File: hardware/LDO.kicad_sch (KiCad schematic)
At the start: 5 parts, among them U1 MCP1826S

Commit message: fixed ERC, made it look pretty
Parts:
- renumbered U1 to U2
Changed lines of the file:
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@@
 		(dnp no)
 		(fields_autoplaced yes)
-		(property "Reference" "U1"
+		(property "Reference" "U2"
 			(at 152.4 56.515 0)
 			(show_name no)
@@
 			(project "PS-HVCarrier"
 				(path "/2365a867-6254-4a7c-9718-f325e0bbac5c/904fa10a-747c-46cf-90d1-33d76069dc5d/d9c02800-502d-4b66-a933-6a0fcb4cc3ad"
-					(reference "U1")
+					(reference "U2")
 					(unit 1)
 				)

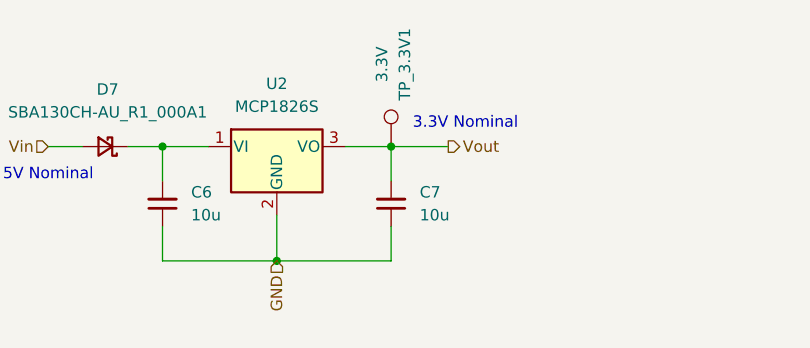
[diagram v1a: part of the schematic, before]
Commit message: updated TP
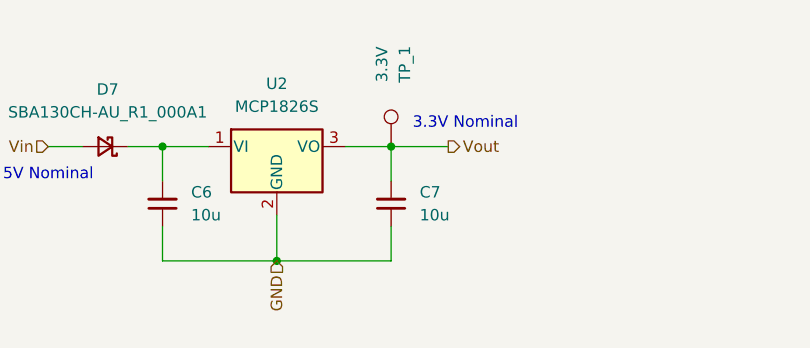
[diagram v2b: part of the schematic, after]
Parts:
- TP_1: renamed from TP_3.3V1; footprint TestPoint:TestPoint_Loop_D1.80mm_Drill1.0mm_Beaded -> TestPoint:TestPoint_THTPad_D3.0mm_Drill1.5mm
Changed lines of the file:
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@@
+			)
+		)
+		(property "LCSC" ""
+			(at 133.35 63.5 0)
+			(hide yes)
+			(show_name no)
+			(do_not_autoplace no)
+			(effects
+				(font
+					(size 1.27 1.27)
+				)
 			)
 		)
@@
 			)
 		)
+		(property "LCSC" ""
+			(at 165.1 69.85 0)
+			(hide yes)
+			(show_name no)
+			(do_not_autoplace no)
+			(effects
+				(font
+					(size 1.27 1.27)
+				)
+			)
+		)
 		(pin "1"
 		)
@@
 		(in_pos_files yes)
 		(dnp no)
-		(property "Reference" "TP_3.3V1"
+		(property "Reference" "TP_1"
 			(at 166.624 54.356 90)
 			(show_name no)
@@
 			)
 		)
-		(property "Footprint" "TestPoint:TestPoint_Loop_D1.80mm_Drill1.0mm_Beaded"
+		(property "Footprint" "TestPoint:TestPoint_THTPad_D3.0mm_Drill1.5mm"
 			(at 170.18 63.5 0)
 			(hide yes)
@@
 		(property "Vf" ""
 			(at 165.1 63.5 0)
+			(show_name no)
+			(do_not_autoplace no)
+			(effects
+				(font
+					(size 1.27 1.27)
+				)
+			)
+		)
+		(property "LCSC" ""
+			(at 165.1 63.5 90)
+			(hide yes)
 			(show_name no)
 			(do_not_autoplace no)
@@
 			(project "PS-HVCarrier"
 				(path "/2365a867-6254-4a7c-9718-f325e0bbac5c/904fa10a-747c-46cf-90d1-33d76069dc5d/d9c02800-502d-4b66-a933-6a0fcb4cc3ad"
-					(reference "TP_3.3V1")
+					(reference "TP_1")
 					(unit 1)
 				)
@@
 			)
 		)
+		(property "LCSC" ""
+			(at 152.4 63.5 0)
+			(hide yes)
+			(show_name no)
+			(do_not_autoplace no)
+			(effects
+				(font
+					(size 1.27 1.27)
+				)
+			)
+		)
 		(pin "2"
 		)
@@
 			(at 139.7 69.85 0)
 			(hide yes)
+			(show_name no)
+			(do_not_autoplace no)
+			(effects
+				(font
+					(size 1.27 1.27)
+				)
+			)
+		)
+		(property "LCSC" ""
+			(at 139.7 69.85 0)
+			(hide yes)

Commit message: added outside test points, removed unncessary symbol fields
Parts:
- C6, C7: Mouser P/N GRM21BR61H106KE43K -> (none)
- D7: Old LCSC P/N C124187 -> (none); Old P/N BAT760-7 -> (none)
- U2: Datasheet Embed kicad-embed://22057B.pdf -> (none); LCSC MFG P/N LM39100S-3.3 -> (none)
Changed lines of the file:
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@@
-			)
-		)
-		(property "Old P/N" "BAT760-7"
-			(at 133.35 63.5 0)
-			(hide yes)
-			(show_name no)
-			(do_not_autoplace no)
-			(effects
-				(font
-					(size 1.27 1.27)
-				)
-			)
-		)
-		(property "Old LCSC P/N" "C124187"
-			(at 133.35 63.5 0)
-			(hide yes)
-			(show_name no)
-			(do_not_autoplace no)
-			(effects
-				(font
-					(size 1.27 1.27)
-				)
-			)
-		)
-		(property "LCSC" ""
-			(at 133.35 63.5 0)
-			(hide yes)
-			(show_name no)
-			(do_not_autoplace no)
-			(effects
-				(font
-					(size 1.27 1.27)
-				)
 			)
 		)
@@
 			)
 		)
-		(property "Mouser P/N" "GRM21BR61H106KE43K"
-			(at 165.1 69.85 0)
-			(hide yes)
-			(show_name no)
-			(do_not_autoplace no)
-			(effects
-				(font
-					(size 1.27 1.27)
-				)
-			)
-		)
 		(property "LCSC P/N" "C440198"
-			(at 165.1 69.85 0)
-			(hide yes)
-			(show_name no)
-			(do_not_autoplace no)
-			(effects
-				(font
-					(size 1.27 1.27)
-				)
-			)
-		)
-		(property "LCSC" ""
 			(at 165.1 69.85 0)
 			(hide yes)
@@
 		(property "Description" "test point"
 			(at 165.1 63.5 0)
-			(hide yes)
-			(show_name no)
-			(do_not_autoplace no)
-			(effects
-				(font
-					(size 1.27 1.27)
-				)
-			)
-		)
-		(property "Color" ""
-			(at 165.1 63.5 0)
-			(show_name no)
-			(do_not_autoplace no)
-			(effects
-				(font
-					(size 1.27 1.27)
-				)
-			)
-		)
-		(property "If" ""
-			(at 165.1 63.5 0)
-			(show_name no)
-			(do_not_autoplace no)
-			(effects
-				(font
-					(size 1.27 1.27)
-				)
-			)
-		)
-		(property "Mfg" ""
-			(at 165.1 63.5 0)
-			(show_name no)
-			(do_not_autoplace no)
-			(effects
-				(font
-					(size 1.27 1.27)
-				)
-			)
-		)
-		(property "Vf" ""
-			(at 165.1 63.5 0)
-			(show_name no)
-			(do_not_autoplace no)
-			(effects
-				(font
-					(size 1.27 1.27)
-				)
-			)
-		)
-		(property "LCSC" ""
-			(at 165.1 63.5 90)
 			(hide yes)
 			(show_name no)
@@
 			)
 		)
-		(property "Datasheet Embed" "kicad-embed://22057B.pdf"
-			(at 152.4 63.5 0)
-			(hide yes)
-			(show_name no)
-			(do_not_autoplace no)
-			(effects
-				(font
-					(size 1.27 1.27)
-				)
-			)
-		)
 		(property "P/N" "MCP1826S-3302E/DB"
 			(at 152.4 63.5 0)
@@
 		)
 		(property "LCSC P/N" "C126055"
-			(at 152.4 63.5 0)
-			(hide yes)
-			(show_name no)
-			(do_not_autoplace no)
-			(effects
-				(font
-					(size 1.27 1.27)
-				)
-			)
-		)
-		(property "LCSC MFG P/N" "LM39100S-3.3"
-			(at 152.4 63.5 0)
-			(hide yes)
-			(show_name no)
-			(do_not_autoplace no)
-			(effects
-				(font
-					(size 1.27 1.27)
-				)
-			)
-		)
-		(property "LCSC" ""
 			(at 152.4 63.5 0)
 			(hide yes)
@@
 			)
 		)
-		(property "Mouser P/N" "GRM21BR61H106KE43K"
-			(at 139.7 69.85 0)
-			(hide yes)
-			(show_name no)
-			(do_not_autoplace no)
-			(effects
-				(font
-					(size 1.27 1.27)
-				)
-			)
-		)
 		(property "LCSC P/N" "C440198"
 			(at 139.7 69.85 0)
 			(hide yes)
-			(show_name no)
-			(do_not_autoplace no)
-			(effects
-				(font
-					(size 1.27 1.27)
-				)
-			)
-		)
-		(property "LCSC" ""
-			(at 139.7 69.85 0)
-			(hide yes)

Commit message: updated kicad sharepoint, added pn
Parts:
- C6, C7: P/N (none) -> GRM21BR61H106KE43K
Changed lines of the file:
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@@
+			)
+		)
+		(property "P/N" "GRM21BR61H106KE43K"
+			(at 165.1 69.85 0)
+			(hide yes)
+			(show_name no)
+			(do_not_autoplace no)
+			(effects
+				(font
+					(size 1.27 1.27)
+				)
 			)
 		)
@@
 			(at 139.7 69.85 0)
 			(hide yes)
+			(show_name no)
+			(do_not_autoplace no)
+			(effects
+				(font
+					(size 1.27 1.27)
+				)
+			)
+		)
+		(property "P/N" "GRM21BR61H106KE43K"
+			(at 139.7 69.85 0)
+			(hide yes)
